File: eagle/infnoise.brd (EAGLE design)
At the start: 31.8 x 13.4 mm, 27 parts, among them SW1 MC74VHC1G66DFT1G, SW2 MC74VHC1G66DFT1G, X1 USBSMT-MALE

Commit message: Changed 100pF caps to 220pF
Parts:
- C7: value 100nF -> 10nF
- C8, C9: value 100pF -> 220pF
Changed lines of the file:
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@@
 <elements>
 <element name="AMP" library="infnoise" package="DFN6-2X3" value="TSV912IQ2T" x="25.7366" y="8.8392" rot="R270"/>
-<element name="C8" library="infnoise" package="0603-CAP" value="100pF" x="23.7046" y="6.604"/>
-<element name="C9" library="infnoise" package="0603-CAP" value="100pF" x="27.159" y="6.5278"/>
+<element name="C8" library="infnoise" package="0603-CAP" value="220pF" x="23.7046" y="6.604"/>
+<element name="C9" library="infnoise" package="0603-CAP" value="220pF" x="27.159" y="6.5278"/>
 <element name="C4" library="infnoise" package="0603-CAP" value="47pF" x="8.2106" y="10.0076" rot="R90"/>
 <element name="C5" library="infnoise" package="0603-CAP" value="47pF" x="9.0742" y="5.461"/>
@@
 <element name="X1" library="infnoise" package="USB-A-SMT-MALE" value="USBSMT-MALE" x="0" y="6.6802" rot="R90"/>
 <element name="R9" library="infnoise" package="0603-RES" value="1K" x="21.463" y="11.684" rot="R180"/>
-<element name="C7" library="infnoise" package="0603-CAP" value="100nF" x="18.0848" y="1.8034" rot="R180"/>
+<element name="C7" library="infnoise" package="0603-CAP" value="10nF" x="18.0848" y="1.8034" rot="R180"/>
 </elements>
 <signals>

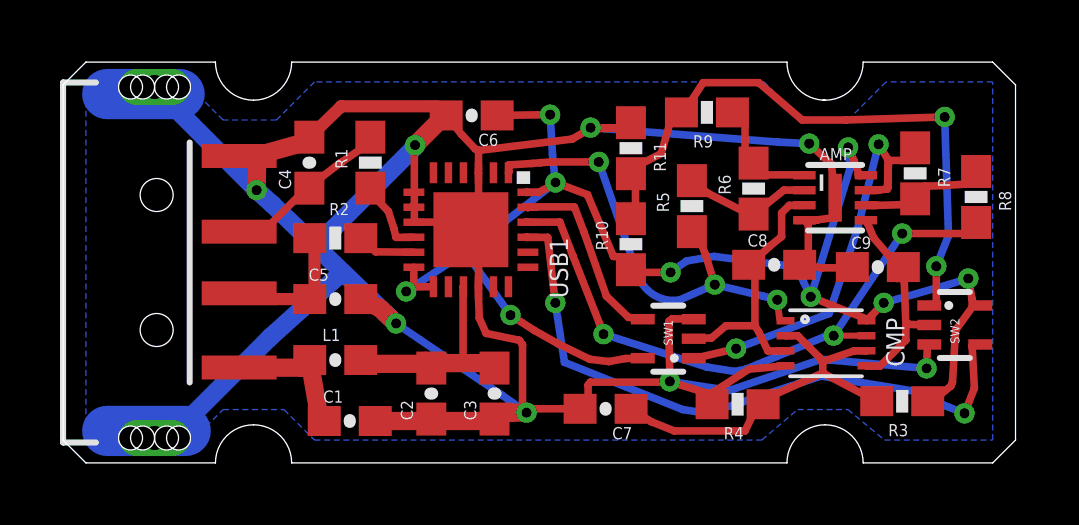
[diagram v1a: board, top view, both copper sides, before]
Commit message: Modified board to remove resistor in feedback, as well as pull-down
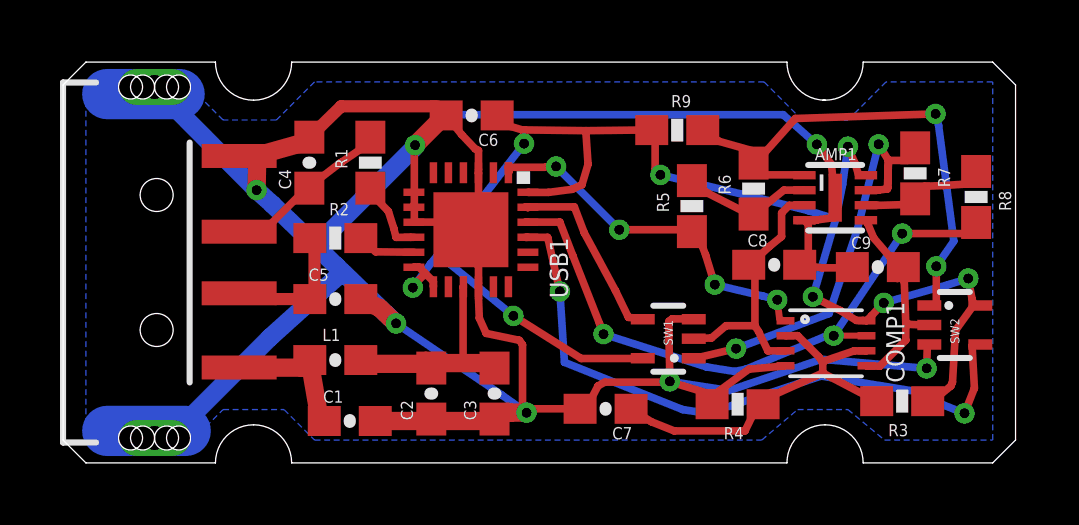
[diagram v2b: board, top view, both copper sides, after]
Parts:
- removed R10: 10K, infnoise:0603-RES
- removed R11: 810K, infnoise:0603-RES
- R9: value 1K -> 10K
- moved R9 1.15 mm to (20.5, 11.1), turned to 0 degrees
- renumbered AMP to AMP1, CMP to COMP1
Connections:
- removed net N$1: AMP1.1, R6.2, R9.1
- net AMP1OUT: now also AMP1.1, R6.2; no longer R10.2, R11.2
- net GND: no longer R11.1
- net VCC33: now also R9.1; no longer R10.1
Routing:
- net AMP1OUT: track 22.4 -> 17.9 mm
- net N$1: track 4.18 -> 0.00 mm
- net COMP1: track 15.1 -> 12.1 mm, vias 3 -> 4
- net GND: track 114.3 -> 113.2 mm, vias 8 -> 7
- net VCC33: track 50.6 -> 51.5 mm, vias 9 -> 8

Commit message: Updated BOM
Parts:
- R6, R7: value 9.76K -> 8.2K
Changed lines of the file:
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@@
 <element name="R1" library="infnoise" package="0603-RES" value="27" x="10.2426" y="10.0076" rot="R90"/>
 <element name="R2" library="infnoise" package="0603-RES" value="27" x="9.0742" y="7.493"/>
-<element name="R6" library="infnoise" package="0603-RES" value="9.76K" x="23.0188" y="9.144" rot="R90"/>
+<element name="R6" library="infnoise" package="0603-RES" value="8.2K" x="23.0188" y="9.144" rot="R90"/>
 <element name="R5" library="infnoise" package="0603-RES" value="10K" x="20.9614" y="8.5598" rot="R90"/>
-<element name="R7" library="infnoise" package="0603-RES" value="9.76K" x="28.4036" y="9.652" rot="R270"/>
+<element name="R7" library="infnoise" package="0603-RES" value="8.2K" x="28.4036" y="9.652" rot="R270"/>
 <element name="R8" library="infnoise" package="0603-RES" value="10K" x="30.4356" y="8.8646" rot="R270"/>
 <element name="R3" library="infnoise" package="0603-RES" value="10K" x="27.9718" y="2.0574" rot="R180"/>

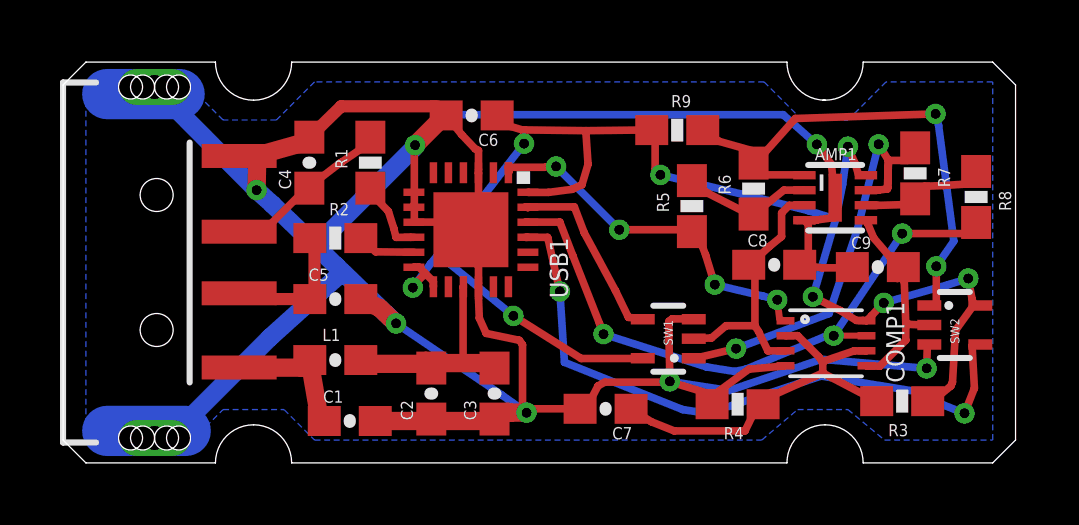
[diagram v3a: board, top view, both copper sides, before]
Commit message: Board clean-up, parts updated from modified library
Schematic:
- Only updated parts from the modified library
Board:
- Moved parts, vias, onto mm grid (was arbitrary?)
- Major re-tracing to keep traces on-grid
- Added full board ground planes (both sides) with grounding vias
scattered around - edges are now fully grounded.
- Moved some parts around beyond grid, e.g. C6 closer to VCCio
- Added 'INFNOISE TRNG' to tNames
Notes:
- Passes ERC and DRC (based on originally included OSHpark Design
Rules), with the exception of the slot pads for the USB connector
(originally approved).
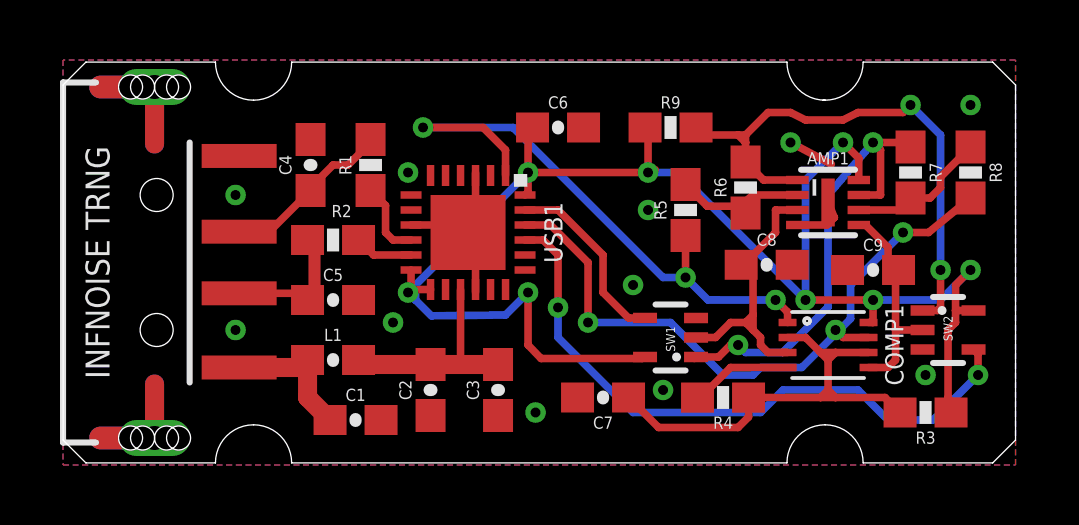
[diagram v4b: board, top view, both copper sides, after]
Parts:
- moved C6 2.91 mm to (16.5, 11.2), turned to 0 degrees
- moved R3 0.86 mm to (28.8, 1.68)
- moved R8 0.84 mm to (30.2, 9.68)
- moved R4 0.53 mm to (22.0, 2.18)
- moved C7 0.39 mm to (18.0, 2.18)
- moved AMP1 0.29 mm to (25.5, 8.68)
- moved SW2 0.28 mm to (29.5, 4.43)
- moved R6 0.27 mm to (22.8, 9.18)
- moved C8 0.25 mm to (23.5, 6.60)
- moved R5 0.25 mm to (20.8, 8.43)
- moved R9 0.24 mm to (20.2, 11.2)
- moved C1 0.20 mm to (9.75, 1.43)
- moved C9 0.19 mm to (27.0, 6.43)
- moved C3 0.17 mm to (14.5, 2.43)
- moved R7 0.16 mm to (28.2, 9.68)
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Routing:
- net GND: track 113.2 -> 27.5 mm, vias 7 -> 11
- net COMP1: track 12.1 -> 20.5 mm, vias 4 -> 3
- net VREF: track 13.0 -> 16.0 mm
- net VCC33: track 51.5 -> 53.1 mm
- net COMP2: track 21.2 -> 22.4 mm
- net VCC: track 9.46 -> 8.30 mm
- net AMP1OUT: track 17.9 -> 19.1 mm
- net B: track 7.82 -> 7.20 mm
- added copper zone on layer 1, net GND
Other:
- board text added: "INFNOISE TRNG"

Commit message: Board layout changed
I moved the components on the board around to give a better visual
representation of the components of the infnoise; USB protection,
filter, divider network, and then where the actual magic happens.  Vias
galore, but ERC and DRC satisfied.
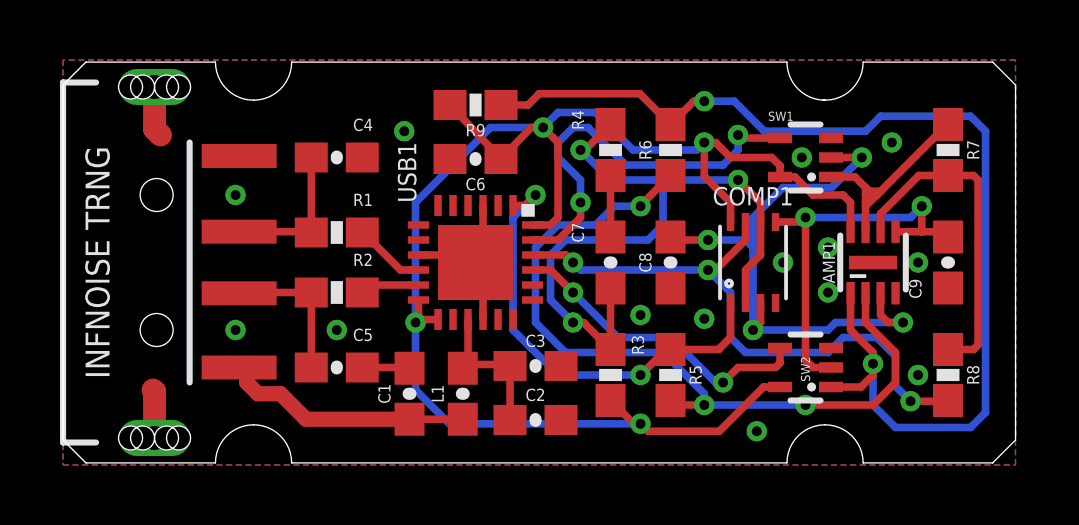
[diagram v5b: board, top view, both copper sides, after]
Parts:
- moved R3 10.6 mm to (18.2, 2.93), turned to 90 degrees
- moved R4 9.06 mm to (18.2, 10.4), turned to 90 degrees
- moved SW1 7.50 mm to (24.8, 10.2)
- moved R8 6.79 mm to (29.5, 2.93)
- moved R9 6.54 mm to (13.8, 11.9), turned to 180 degrees
- moved R5 5.52 mm to (20.2, 2.93), turned to 270 degrees
- moved SW2 4.91 mm to (24.8, 3.18), turned to 90 degrees
- moved C7 4.51 mm to (18.2, 6.68), turned to 90 degrees
- moved L1 4.47 mm to (13.3, 2.31), turned to 90 degrees
- moved COMP1 3.72 mm to (23.0, 6.68), turned to 0 degrees
- moved C2 3.64 mm to (15.8, 1.43), turned to 0 degrees
- moved C8 3.21 mm to (20.2, 6.68), turned to 90 degrees
- moved C6 2.94 mm to (13.8, 10.1), turned to 180 degrees
- moved R6 2.80 mm to (20.2, 10.4)
- moved R1 2.52 mm to (9.12, 7.68), turned to 0 degrees
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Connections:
- net A: now also C8.2; no longer C8.1
- net AMP1OUT: now also R9.1; no longer R9.2
- net GND: now also C2.2, C3.2, C8.1, R4.1; no longer C2.1, C3.1, C8.2, R4.2
- net N$2: now also R1.2; no longer R1.1
- net USB_P: now also R1.1; no longer R1.2
- net VCC: now also C2.1, C3.1; no longer C2.2, C3.2
- net VCC33: now also R9.2; no longer R9.1
- net VREF: now also R4.2; no longer R4.1
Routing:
- net FB1: track 4.74 -> 26.4 mm, vias 0 -> 3
- net AMP1OUT: track 19.1 -> 37.5 mm
- net GND: track 27.5 -> 12.9 mm, vias 11 -> 14
- net A: track 9.63 -> 20.4 mm, vias 0 -> 4
- net SW2EN: track 21.4 -> 10.6 mm
- net VREF: track 16.0 -> 24.2 mm, vias 0 -> 3
- net AMP2OUT: track 15.5 -> 8.14 mm, vias 2 -> 0
- net SW1EN: track 6.32 -> 13.6 mm, vias 0 -> 2
- net B: track 7.20 -> 13.5 mm, vias 0 -> 2
- net FB2: track 4.91 -> 11.0 mm
- net COMP1: track 20.5 -> 15.2 mm, vias 3 -> 2
- net VCCIN: track 4.59 -> 8.31 mm
- net VCC: track 8.30 -> 4.92 mm
- net COMP2: track 22.4 -> 20.0 mm
- net VCC33: track 53.1 -> 52.2 mm, vias 8 -> 4
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
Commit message: Added 3 fiducial marks on the board
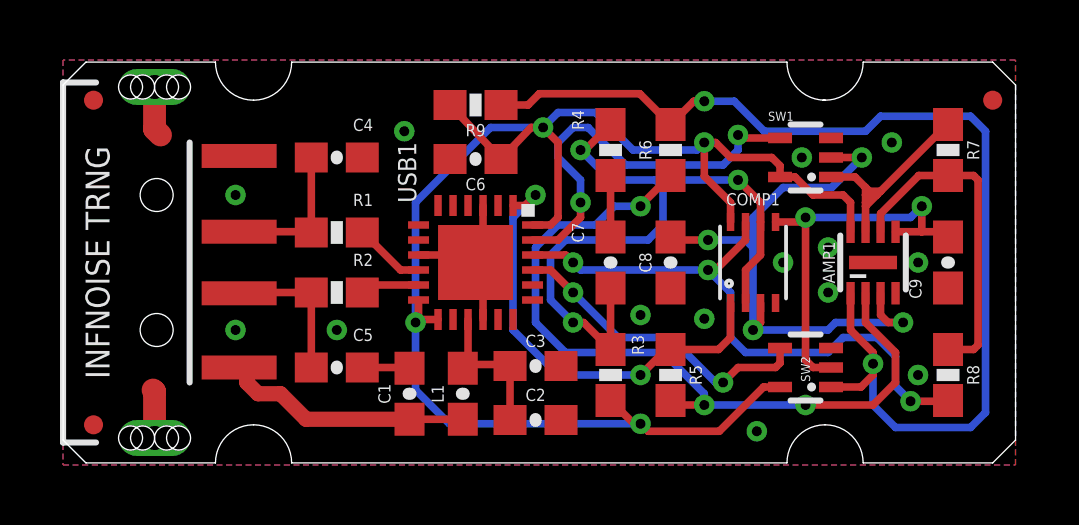
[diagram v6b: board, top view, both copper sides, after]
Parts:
- added FID1, FID2, FID3: FIDUCIALUFIDUCIAL, SparkFun-Aesthetics:MICRO-FIDUCIAL
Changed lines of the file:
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@@
 <?xml version="1.0" encoding="utf-8"?>
 <!DOCTYPE eagle SYSTEM "eagle.dtd">
-<eagle version="6.5.0">
+<eagle version="7.1.0">
 <drawing>
 <settings>
@@
 <setting verticaltext="up"/>
 </settings>
-<grid distance="0.5" unitdist="mm" unit="mm" style="lines" multiple="1" display="yes" altdistance="0.125" altunitdist="mm" altunit="mm"/>
+<grid distance="0.01" unitdist="inch" unit="inch" style="lines" multiple="1" display="yes" altdistance="0.125" altunitdist="mm" altunit="mm"/>
 <layers>
-<layer number="1" name="Top" color="4" fill="1" visible="yes" active="yes"/>
-<layer number="16" name="Bottom" color="1" fill="1" visible="yes" active="yes"/>
+<layer number="1" name="Top" color="4" fill="1" visible="no" active="yes"/>
+<layer number="16" name="Bottom" color="1" fill="1" visible="no" active="yes"/>
 <layer number="17" name="Pads" color="2" fill="1" visible="yes" active="yes"/>
 <layer number="18" name="Vias" color="2" fill="1" visible="yes" active="yes"/>
@@
 <layer number="48" name="Document" color="7" fill="1" visible="yes" active="yes"/>
 <layer number="49" name="Reference" color="7" fill="1" visible="yes" active="yes"/>
+<layer number="50" name="dxf" color="7" fill="1" visible="no" active="no"/>
 <layer number="51" name="tDocu" color="7" fill="1" visible="yes" active="yes"/>
 <layer number="52" name="bDocu" color="7" fill="1" visible="yes" active="yes"/>
+<layer number="53" name="tGND_GNDA" color="7" fill="9" visible="no" active="no"/>
+<layer number="54" name="bGND_GNDA" color="1" fill="9" visible="no" active="no"/>
+<layer number="56" name="wert" color="7" fill="1" visible="no" active="no"/>
 <layer number="90" name="Modules" color="5" fill="1" visible="no" active="no"/>
 <layer number="91" name="Nets" color="2" fill="1" visible="no" active="no"/>
@@
 <layer number="97" name="Info" color="7" fill="1" visible="no" active="no"/>
 <layer number="98" name="Guide" color="6" fill="1" visible="no" active="no"/>
+<layer number="100" name="Muster" color="7" fill="1" visible="no" active="no"/>
+<layer number="101" name="Patch_Top" color="12" fill="4" visible="yes" active="yes"/>
+<layer number="102" name="Vscore" color="7" fill="1" visible="yes" active="yes"/>
+<layer number="103" name="tMap" color="7" fill="1" visible="yes" active="yes"/>
+<layer number="104" name="Name" color="16" fill="1" visible="yes" active="yes"/>
+<layer number="105" name="tPlate" color="7" fill="1" visible="yes" active="yes"/>
+<layer number="106" name="bPlate" color="7" fill="1" visible="yes" active="yes"/>
+<layer number="107" name="Crop" color="7" fill="1" visible="yes" active="yes"/>
+<layer number="108" name="tplace-old" color="10" fill="1" visible="no" active="yes"/>
+<layer number="109" name="ref-old" color="11" fill="1" visible="no" active="yes"/>
+<layer number="116" name="Patch_BOT" color="9" fill="4" visible="yes" active="yes"/>
+<layer number="121" name="_tsilk" color="7" fill="1" visible="yes" active="yes"/>
+<layer number="122" name="_bsilk" color="7" fill="1" visible="yes" active="yes"/>
+<layer number="125" name="_tNames" color="7" fill="1" visible="yes" active="yes"/>
+<layer number="144" name="Drill_legend" color="7" fill="1" visible="yes" active="yes"/>
+<layer number="151" name="HeatSink" color="7" fill="1" visible="yes" active="yes"/>
+<layer number="199" name="Contour" color="7" fill="1" visible="yes" active="yes"/>
+<layer number="200" name="200bmp" color="1" fill="10" visible="yes" active="yes"/>
+<layer number="201" name="201bmp" color="2" fill="10" visible="yes" active="yes"/>
+<layer number="202" name="202bmp" color="3" fill="10" visible="yes" active="yes"/>
+<layer number="203" name="203bmp" color="4" fill="10" visible="yes" active="yes"/>
+<layer number="204" name="204bmp" color="5" fill="10" visible="yes" active="yes"/>
+<layer number="205" name="205bmp" color="6" fill="10" visible="yes" active="yes"/>
+<layer number="206" name="206bmp" color="7" fill="10" visible="yes" active="yes"/>
+<layer number="207" name="207bmp" color="8" fill="10" visible="yes" active="yes"/>
+<layer number="208" name="208bmp" color="9" fill="10" visible="yes" active="yes"/>
+<layer number="209" name="209bmp" color="7" fill="1" visible="yes" active="yes"/>
+<layer number="210" name="210bmp" color="7" fill="1" visible="yes" active="yes"/>
+<layer number="211" name="211bmp" color="7" fill="1" visible="yes" active="yes"/>
+<layer number="212" name="212bmp" color="7" fill="1" visible="yes" active="yes"/>
+<layer number="213" name="213bmp" color="7" fill="1" visible="yes" active="yes"/>
+<layer number="214" name="214bmp" color="7" fill="1" visible="yes" active="yes"/>
+<layer number="215" name="215bmp" color="7" fill="1" visible="yes" active="yes"/>
+<layer number="216" name="216bmp" color="7" fill="1" visible="yes" active="yes"/>
+<layer number="217" name="217bmp" color="18" fill="1" visible="no" active="no"/>
+<layer number="218" name="218bmp" color="19" fill="1" visible="no" active="no"/>
+<layer number="219" name="219bmp" color="20" fill="1" visible="no" active="no"/>
+<layer number="220" name="220bmp" color="21" fill="1" visible="no" active="no"/>
+<layer number="221" name="221bmp" color="22" fill="1" visible="no" active="no"/>
+<layer number="222" name="222bmp" color="23" fill="1" visible="no" active="no"/>
+<layer number="223" name="223bmp" color="24" fill="1" visible="no" active="no"/>
+<layer number="224" name="224bmp" color="25" fill="1" visible="no" active="no"/>
+<layer number="250" name="Descript" color="3" fill="1" visible="no" active="no"/>
+<layer number="251" name="SMDround" color="12" fill="11" visible="no" active="no"/>
+<layer number="254" name="cooling" color="7" fill="1" visible="yes" active="yes"/>
 </layers>
 <board>
@@
 <pass name="Default">
 <param name="RoutingGrid" value="50mil"/>
+<param name="AutoGrid" value="1"/>
+<param name="Efforts" value="0"/>
+<param name="TopRouterVariant" value="1"/>
 <param name="tpViaShape" value="round"/>
 <param name="PrefDir.1" value="|"/>
@@
 <attribute name="NAME" x="17.365" y="7.6802" size="0.4064" layer="25" font="vector" rot="R90" align="bottom-center"/>
 </element>
+<element name="FID1" library="SparkFun-Aesthetics" package="MICRO-FIDUCIAL" value="FIDUCIALUFIDUCIAL" x="1.016" y="1.27"/>
+<element name="FID2" library="SparkFun-Aesthetics" package="MICRO-FIDUCIAL" value="FIDUCIALUFIDUCIAL" x="1.016" y="12.0904"/>
+<element name="FID3" library="SparkFun-Aesthetics" package="MICRO-FIDUCIAL" value="FIDUCIALUFIDUCIAL" x="30.988" y="12.0904"/>
 </elements>
 <signals>

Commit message: Made 0.5mm pads all the same size and shrank QFN24 center pad
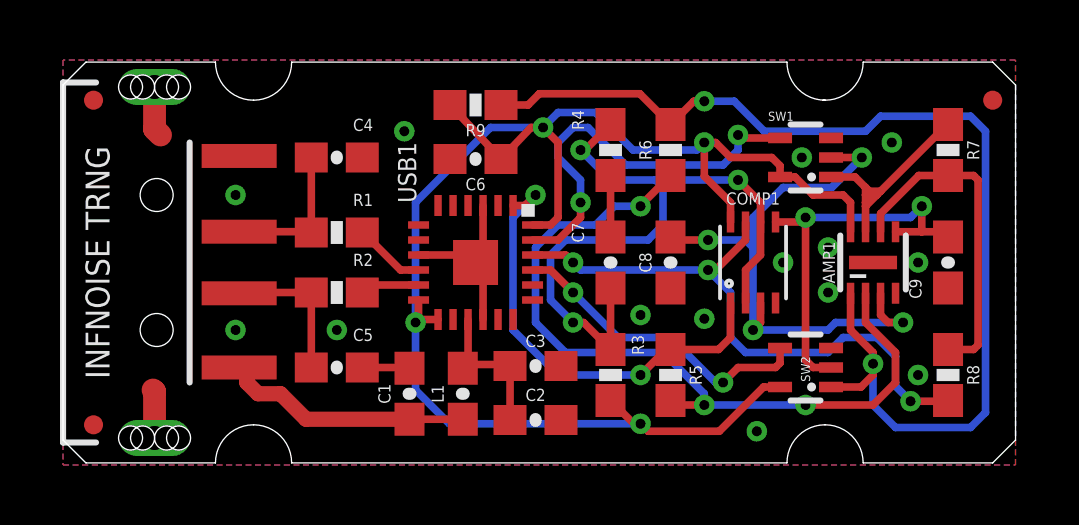
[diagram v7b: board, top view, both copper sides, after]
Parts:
- AMP1: device infnoise:DFN6-2X3 -> infnoise:DFN8-2X3
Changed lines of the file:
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@@
 </autorouter>
 <elements>
-<element name="AMP1" library="infnoise" package="DFN6-2X3" value="TSV912IQ2T" x="27" y="6.6802"/>
+<element name="AMP1" library="infnoise" package="DFN8-2X3" value="TSV912IQ2T" x="27" y="6.6802"/>
 <element name="C8" library="infnoise" package="0603-CAP" value="220pF" x="20.25" y="6.6802" rot="R90"/>
 <element name="C9" library="infnoise" package="0603-CAP" value="220pF" x="29.5" y="6.6802" smashed="yes" rot="R90">
